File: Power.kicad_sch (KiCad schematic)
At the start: 20 parts, among them J1 B2B-PH-SM4-TBLFSN, U4 BQ25185DLHR, U5 MCP1727T-3302E/SN

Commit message: Initial complete implementation of LEDS.
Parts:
- added C7: GRM21BZ71E106KE15L, Hourglass_footprint_library:CAP_GRM21BZ_MUR, symbol Hourglass_symbol_library:GRM21BZ71E106KE15L
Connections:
- net GND: now also C7.2
- net at C3.1, U4.1 (SYS), U5.1 (VIN)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: now also C7.1
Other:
- note added: "Vsys Outut Reg 4.5V or Vbat"
- note removed: "Vsys Outut 4.5V"
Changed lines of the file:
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@@
 		)
 	)
-	(text "Vsys Outut 4.5V"
+	(text "Vsys Outut Reg 4.5V or Vbat\n"
 		(exclude_from_sim yes)
-		(at 124.714 116.332 0)
+		(at 130.302 108.204 0)
 		(effects
 			(font
@@
 	)
 	(junction
+		(at 128.27 111.76)
+		(diameter 0)
+		(color 0 0 0 0)
+	)
+	(junction
 		(at 40.64 123.19)
 		(diameter 0)
@@
 	(wire
 		(pts
+			(xy 128.27 111.76) (xy 128.27 118.11)
+		)
+		(stroke
+			(width 0)
+			(type default)
+		)
+	)
+	(wire
+		(pts
 			(xy 177.8 38.1) (xy 177.8 43.18)
 		)
@@
 	(wire
 		(pts
-			(xy 121.92 111.76) (xy 168.91 111.76)
+			(xy 121.92 111.76) (xy 128.27 111.76)
 		)
 		(stroke
@@
 	(wire
 		(pts
+			(xy 128.27 125.73) (xy 128.27 142.24)
+		)
+		(stroke
+			(width 0)
+			(type default)
+		)
+	)
+	(wire
+		(pts
 			(xy 146.05 100.33) (xy 146.05 102.87)
 		)
@@
 	(wire
 		(pts
+			(xy 128.27 111.76) (xy 168.91 111.76)
+		)
+		(stroke
+			(width 0)
+			(type default)
+		)
+	)
+	(wire
+		(pts
 			(xy 40.64 139.7) (xy 50.8 139.7)
 		)
@@
 	)
 	(symbol
+		(lib_id "Hourglass_symbol_library:GRM21BZ71E106KE15L")
+		(at 128.27 121.92 270)
+		(unit 1)
+		(exclude_from_sim no)
+		(in_bom yes)
+		(on_board yes)
+		(dnp no)
+		(property "Reference" "C7"
+			(at 130.81 122.1739 90)
+			(effects
+				(font
+					(size 1.524 1.524)
+				)
+				(justify left)
+			)
+		)
+		(property "Value" "GRM21BZ71E106KE15L"
+			(at 132.08 123.1899 90)
+			(effects
+				(font
+					(size 1.524 1.524)
+				)
+				(justify left)
+				(hide yes)
+			)
+		)
+		(property "Footprint" "Hourglass_footprint_library:CAP_GRM21BZ_MUR"
+			(at 119.126 121.92 0)
+			(effects
+				(font
+					(size 1.27 1.27)
+					(italic yes)
+				)
+				(hide yes)
+			)
+		)
+		(property "Datasheet" "https://search.murata.co.jp/Ceramy/image/img/A01X/G101/ENG/GRM21BZ71E106KE15-01.pdf"
+			(at 134.62 121.92 0)
+			(effects
+				(font
+					(size 1.27 1.27)
+					(italic yes)
+				)
+				(hide yes)
+			)
+		)
+		(property "Description" "CAP CER 10UF 25V X7R 0805"
+			(at 128.27 121.92 0)
+			(effects
+				(font
+					(size 1.27 1.27)
+				)
+				(hide yes)
+			)
+		)
+		(pin "1"
+		)
+		(pin "2"
+		)
+		(instances
+			(project "Hourglass_PCBA"
+				(path "/a75630d2-15a7-42bc-8ce0-7846cbd1da6b/b64ac316-366b-4dad-aacf-d60ea5acbc88"
+					(reference "C7")
+					(unit 1)
+				)
+			)
+		)
+	)
+	(symbol
 		(lib_id "power:GND")
 		(at 30.48 142.24 0)
@@
 	)
 	(symbol
+		(lib_id "power:GND")
+		(at 128.27 142.24 0)
+		(unit 1)
+		(exclude_from_sim no)
+		(in_bom yes)
+		(on_board yes)
+		(dnp no)
+		(fields_autoplaced yes)
+		(property "Reference" "#PWR32"
+			(at 128.27 148.59 0)
+			(effects
+				(font
+					(size 1.27 1.27)
+				)
+				(hide yes)
+			)
+		)
+		(property "Value" "GND"
+			(at 128.27 147.32 0)
+			(effects
+				(font
+					(size 1.27 1.27)
+				)
+			)
+		)
+		(property "Footprint" ""
+			(at 128.27 142.24 0)
+			(effects
+				(font
+					(size 1.27 1.27)
+				)
+				(hide yes)
+			)
+		)
+		(property "Datasheet" ""
+			(at 128.27 142.24 0)
+			(effects
+				(font
+					(size 1.27 1.27)
+				)
+				(hide yes)
+			)
+		)
+		(property "Description" "Power symbol creates a global label with name \"GND\" , ground"
+			(at 128.27 142.24 0)
+			(effects
+				(font
+					(size 1.27 1.27)
+				)
+				(hide yes)
+			)
+		)
+		(pin "1"
+		)
+		(instances
+			(project "Hourglass_PCBA"
+				(path "/a75630d2-15a7-42bc-8ce0-7846cbd1da6b/b64ac316-366b-4dad-aacf-d60ea5acbc88"
+					(reference "#PWR32")
+					(unit 1)
+				)
+			)
+		)
+	)
+	(symbol
 		(lib_id "Hourglass_symbol_library:SR0805JR-0710KL")
 		(at 50.8 130.81 90)
@@
 			)
 		)
-		(property "Datasheet" "BQ25185DLHR"
+		(property "Datasheet" "https://www.ti.com/lit/ds/symlink/bq25185.pdf?ts=1701339761812&ref_url=https%253A%252F%252Fwww.ti.com%252Fproduct%252FBQ25185"
 			(at 84.836 138.176 0)
 			(effects
@@
 			)
 		)
-		(property "Datasheet" "MCP1727T-3302E/SN"
+		(property "Datasheet" "https://ww1.microchip.com/downloads/en/DeviceDoc/21999b.pdf"
 			(at 194.564 127 0)
 			(effects

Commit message: Completed schematic for MCU section
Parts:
- removed R5: SR0805JR-0710KL, Hourglass_footprint_library:SR0805JR-0710KL, symbol Hourglass_symbol_library:SR0805JR-0710KL
- added R5: RMCF0805FT10K0, Hourglass_footprint_library:RMCF0805FT10K0, symbol Hourglass_symbol_library:RMCF0805FT10K0
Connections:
- net GND: now also R5.
- net at U4.6 (TS/MR): now also R5.
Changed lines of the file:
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@@
+	)
+	(symbol
+		(lib_name "RMCF0805FT10K0_1")
+		(lib_id "Hourglass_symbol_library:RMCF0805FT10K0")
+		(at 50.8 130.81 90)
+		(unit 1)
+		(exclude_from_sim no)
+		(in_bom yes)
+		(on_board yes)
+		(dnp no)
+		(property "Reference" "R5"
+			(at 52.07 128.0158 90)
+			(effects
+				(font
+					(size 1.27 1.27)
+				)
+				(justify right)
+			)
+		)
+		(property "Value" "RMCF0805FT10K0"
+			(at 47.752 122.9358 0)
+			(effects
+				(font
+					(size 1.27 1.27)
+				)
+				(justify right)
+				(hide yes)
+			)
+		)
+		(property "Footprint" "Hourglass_footprint_library:RMCF0805FT10K0"
+			(at 55.118 130.048 0)
+			(effects
+				(font
+					(size 1.27 1.27)
+				)
+				(hide yes)
+			)
+		)
+		(property "Datasheet" "https://www.seielect.com/catalog/sei-rmcf_rmcp.pdf"
+			(at 56.896 130.048 0)
+			(effects
+				(font
+					(size 1.27 1.27)
+				)
+				(hide yes)
+			)
+		)
+		(property "Description" "RES 10K OHM 1% 1/8W 0805"
+			(at 44.196 129.54 0)
+			(effects
+				(font
+					(size 1.27 1.27)
+				)
+				(hide yes)
+			)
+		)
+		(pin ""
+		)
+		(pin ""
+		)
+		(instances
+			(project ""
+				(path "/a75630d2-15a7-42bc-8ce0-7846cbd1da6b/b64ac316-366b-4dad-aacf-d60ea5acbc88"
+					(reference "R5")
+					(unit 1)
+				)
+			)
+		)
 	)
 	(symbol
@@
 					(unit 1)
 				)
-			)
-		)
-	)
-	(symbol
-		(lib_id "Hourglass_symbol_library:SR0805JR-0710KL")
-		(at 50.8 130.81 90)
-		(unit 1)
-		(exclude_from_sim no)
-		(in_bom yes)
-		(on_board yes)
-		(dnp no)
-		(property "Reference" "R5"
-			(at 48.26 129.5399 0)
-			(effects
-				(font
-					(size 1.27 1.27)
-				)
-				(justify right)
-			)
-		)
-		(property "Value" "SR0805JR-0710KL"
-			(at 55.88 132.0799 90)
-			(effects
-				(font
-					(size 1.27 1.27)
-				)
-				(justify right)
-				(hide yes)
-			)
-		)
-		(property "Footprint" "Hourglass_footprint_library:SR0805JR-0710KL"
-			(at 55.372 130.81 0)
-			(effects
-				(font
-					(size 1.27 1.27)
-				)
-				(hide yes)
-			)
-		)
-		(property "Datasheet" "https://www.yageo.com/upload/media/product/app/datasheet/rchip/pyu-sr_20105_rohs_l.pdf"
-			(at 59.182 130.556 0)
-			(effects
-				(font
-					(size 1.27 1.27)
-				)
-				(hide yes)
-			)
-		)
-		(property "Description" "RES 10K OHM 5% 1/8W 0805"
-			(at 45.974 130.81 0)
-			(effects
-				(font
-					(size 1.27 1.27)
-				)
-				(hide yes)
-			)
-		)
-		(pin ""
-		)
-		(pin ""
-		)
-		(instances
-			(project ""
-				(path "/a75630d2-15a7-42bc-8ce0-7846cbd1da6b/b64ac316-366b-4dad-aacf-d60ea5acbc88"
-					(reference "R5")
-					(unit 1)
-				)

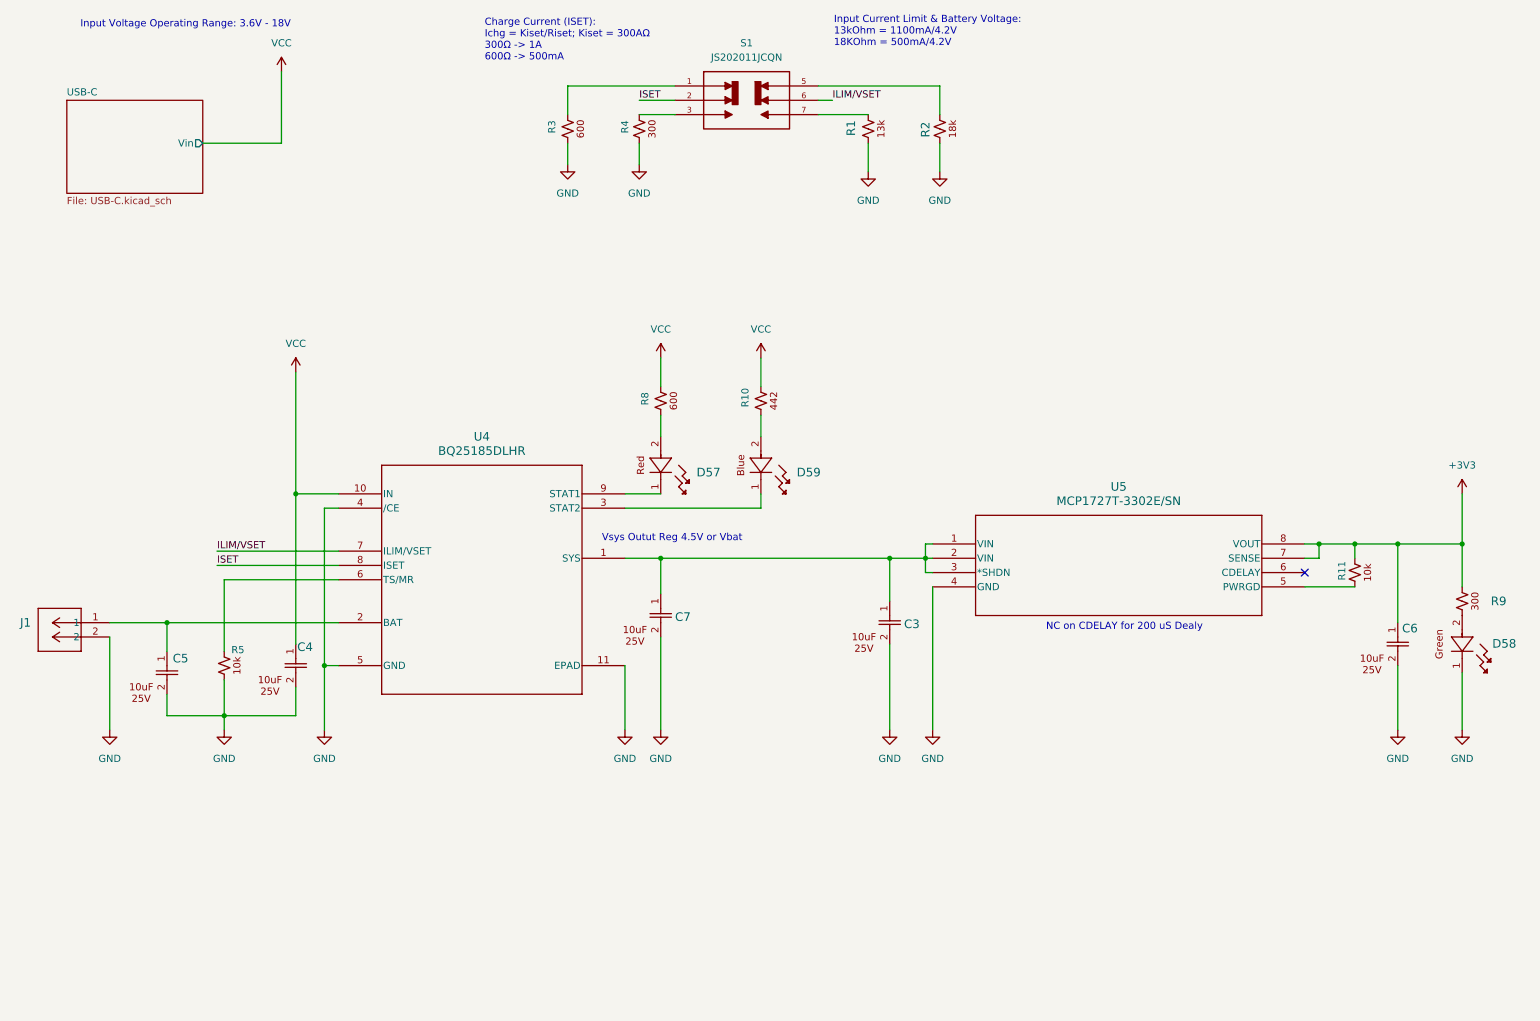
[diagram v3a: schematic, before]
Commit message: First complete schematic with TPs.
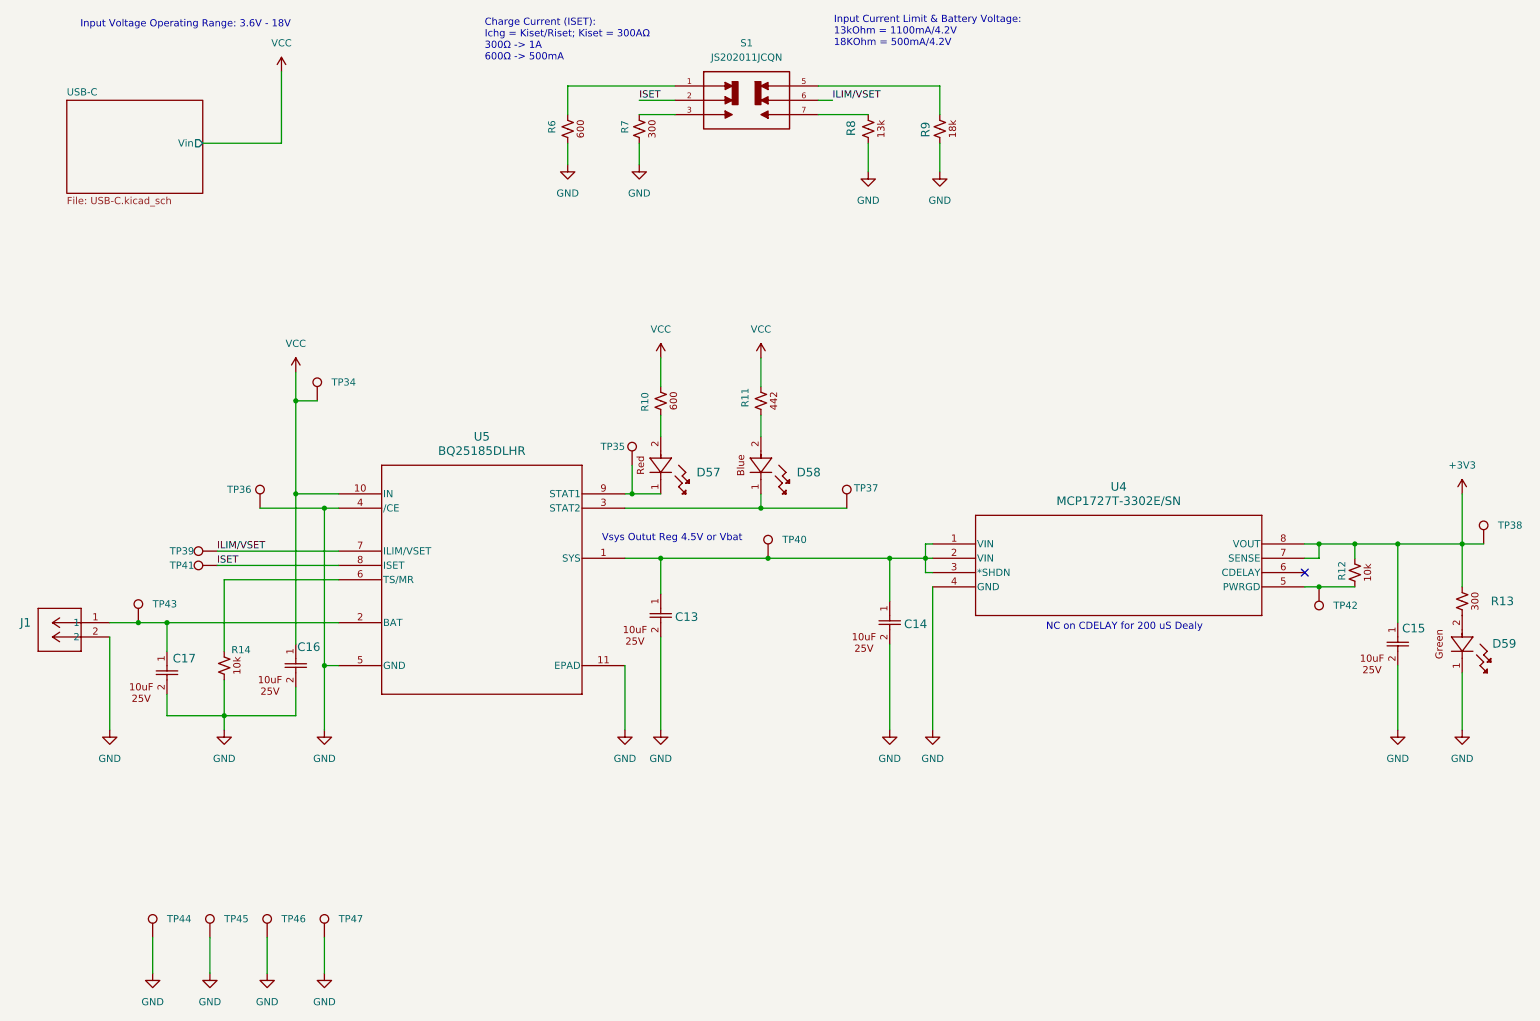
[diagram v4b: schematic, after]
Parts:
- added TP34, TP35, TP36, TP37, TP38, TP39, TP40, TP41, TP42, TP43, TP44, TP45, TP46, TP47: TestPoint, TestPoint:TestPoint_Pad_D1.0mm, symbol Connector:TestPoint
- renumbered C7 to C13, C3 to C14, C6 to C15, C4 to C16, C5 to C17, D59 to D58, D58 to D59, R8 to R10, R10 to R11, R11 to R12, R9 to R13, R5 to R14, R3 to R6, R4 to R7, R1 to R8, R2 to R9, U5 to U4, U4 to U5
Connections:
- net +3V3: now also TP38.1
- net GND: now also TP36.1, TP44.1, TP45.1, TP46.1, TP47.1
- net ILIM/VSET: now also TP39.1
- net ISET: now also TP41.1
- net VCC: now also TP34.1
- net at R12., U4.5 (PWRGD): now also TP42.1
- net at C17.1, J1.1, U5.2 (BAT): now also TP43.1
- net at C13.1, C14.1, U4.1 (VIN)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: now also TP40.1
- net at D57.1, U5.9 (STAT1): now also TP35.1
- net at D58.1, U5.3 (STAT2): now also TP37.1

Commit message: Addressed DRC warnings and errors.
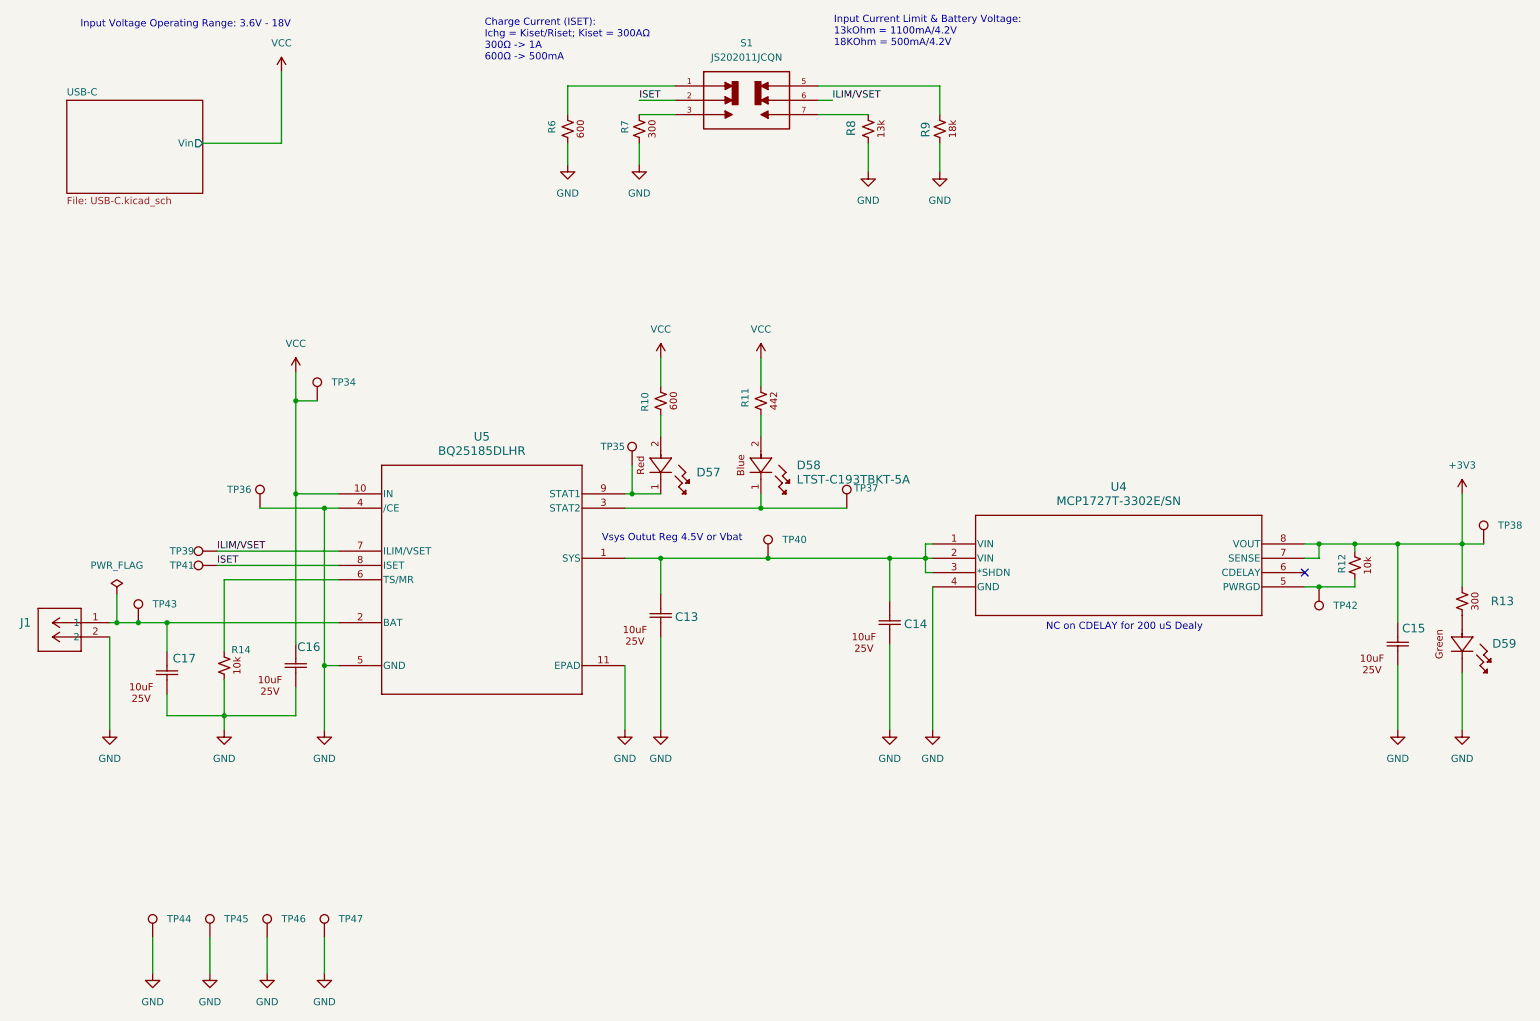
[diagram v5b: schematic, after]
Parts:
- R10, R6: footprint Hourglass_footprint_library:MCU08050C6000FP500 -> Hourglass_footprint_library:RESC2012X55N
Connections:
- net +3V3: now also R12.2, R13.2; no longer R12., R13.
- net GND: now also D59.2, R14.1, R6.1, R7.1, R8.1, R9.1; no longer D59.1, R14., R6., R7., R8., R9.
- net VCC: now also R10.2, R11.2; no longer R10., R11.
- net at TP42.1, U4.5 (PWRGD): now also R12.1; no longer R12.
- net at U5.6 (TS/MR): now also R14.2; no longer R14.
- net at S1.1: now also R6.2; no longer R6.
- net at S1.3: now also R7.2; no longer R7.
- net at S1.5: now also R9.2; no longer R9.
- net at S1.7: now also R8.2; no longer R8.
- net at D58.2: now also R11.1; no longer R11.
- net at D57.2: now also R10.1; no longer R10.
- new net: D59.1, R13.1
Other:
- moved on the sheet: R12

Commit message: Added comments on schematic and fixed bus for SW[0..4] on Bot LEDs.
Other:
- note added: "BAT to SYS Max Current: 3.125 A"
- note added: "IN to SYS Max Current: 1.1 A"
- note added: "Iout Min: 1.5A"
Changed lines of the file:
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@@
+		)
+	)
+	(text "BAT to SYS Max Current: 3.125 A\n"
+		(exclude_from_sim yes)
+		(at 97.282 142.24 0)
+		(effects
+			(font
+				(size 1.27 1.27)
+			)
+		)
+	)
+	(text "Iout Min: 1.5A"
+		(exclude_from_sim yes)
+		(at 243.078 105.41 0)
+		(effects
+			(font
+				(size 1.27 1.27)
+			)
+		)
+	)
+	(text "IN to SYS Max Current: 1.1 A"
+		(exclude_from_sim yes)
+		(at 96.52 139.7 0)
+		(effects
+			(font
+				(size 1.27 1.27)
+			)
 		)
 	)

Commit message: Re-annotated entire schematic.
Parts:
- renumbered R9 to R10, R10 to R11, R11 to R12, R12 to R13, R13 to R14, R14 to R15, R6 to R7, R7 to R8, R8 to R9, TP34 to TP37, TP35 to TP38, TP36 to TP39, TP37 to TP40, TP38 to TP41, TP39 to TP42, TP40 to TP43, TP41 to TP44, TP42 to TP45, TP43 to TP46, TP44 to TP47, TP45 to TP48, TP46 to TP49, TP47 to TP50
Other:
- note added: "NC on CDELAY for 200 uS Delay"
- note removed: "NC on CDELAY for 200 uS Dealy"
- title: (none) -> Hourglass
